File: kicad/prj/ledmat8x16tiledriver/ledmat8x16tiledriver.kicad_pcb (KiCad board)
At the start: 4 copper layers, 31.9 x 31.9 mm, 15 parts, among them J3 Conn_02x08_Odd_Even, J4 Conn_02x08_Odd_Even, U2 DMP31D7LDW, U3 DMP31D7LDW, U4 DMP31D7LDW, U5 DMP31D7LDW

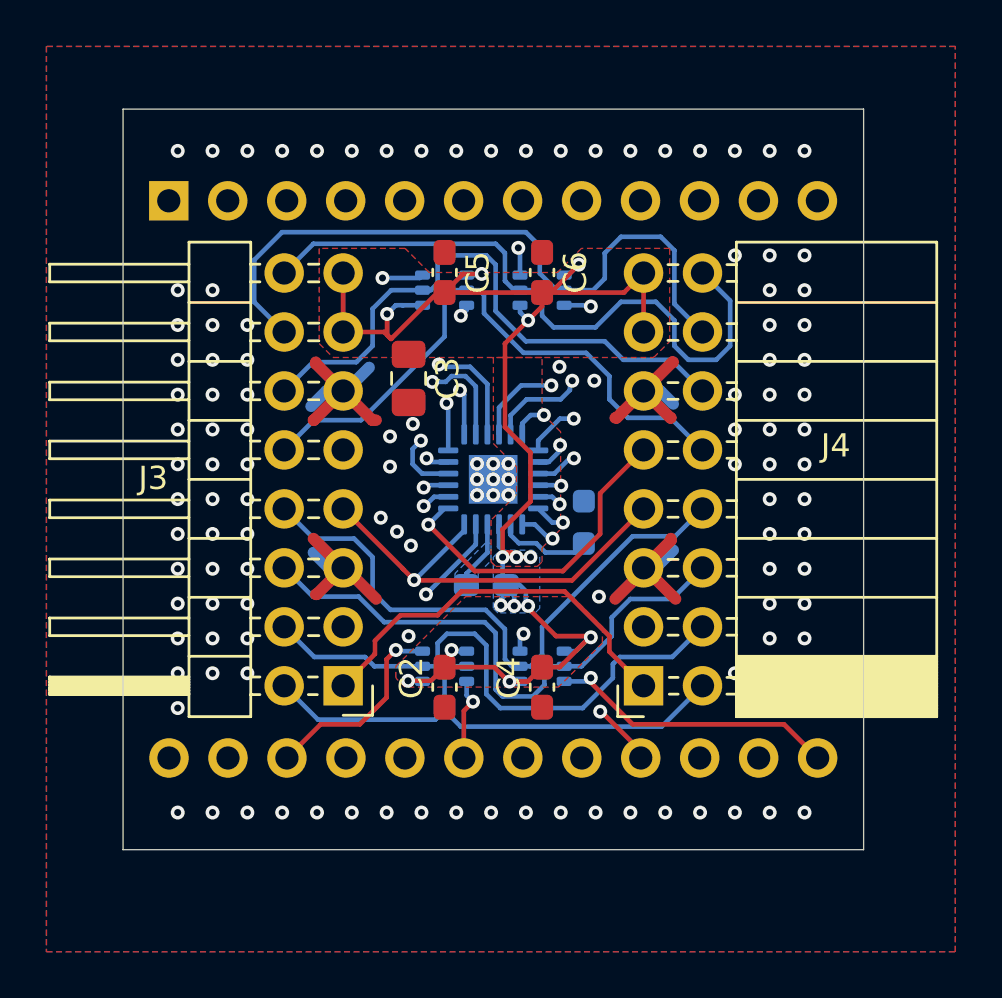
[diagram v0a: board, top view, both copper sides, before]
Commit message: re-route traces close to clock trace
Clock appeared to couple into the closeby traces
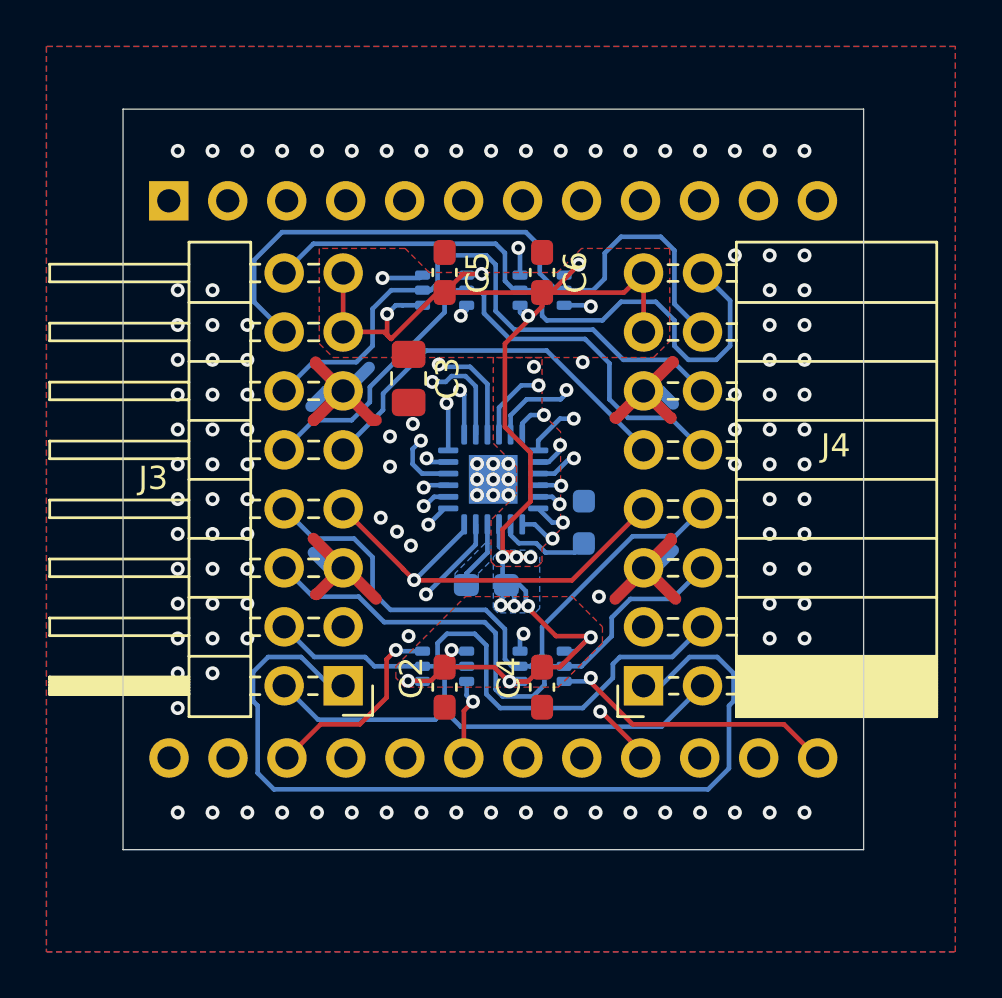
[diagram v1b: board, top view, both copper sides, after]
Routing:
- net /BLANK: track 41.3 -> 63.1 mm
- net /LAT: track 19.4 -> 23.1 mm
- net GND: vias 126 -> 124

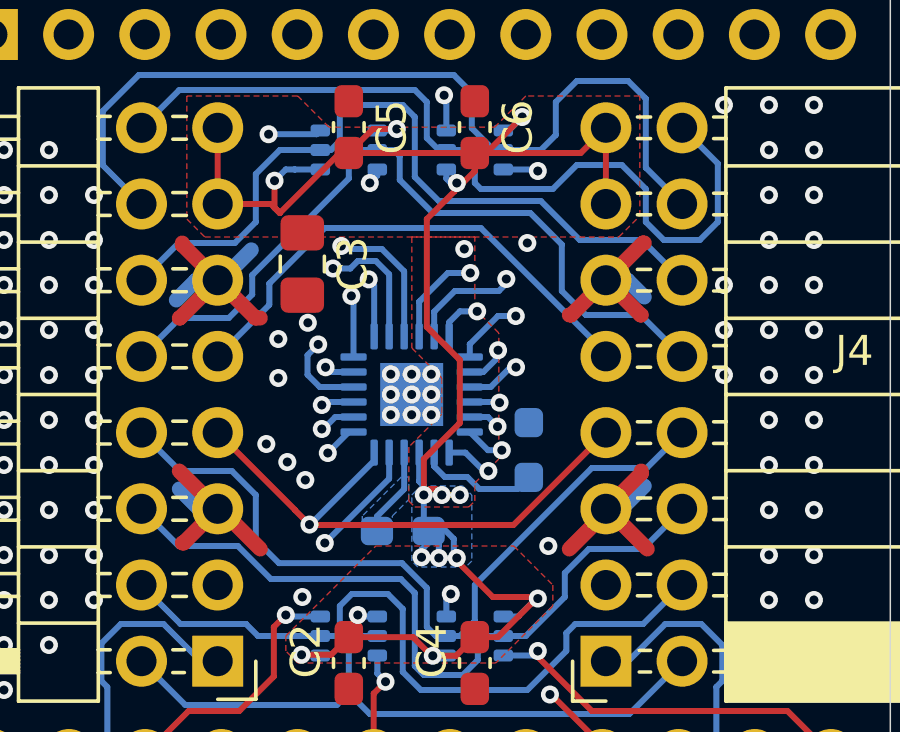
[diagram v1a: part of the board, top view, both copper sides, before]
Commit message: attempt to increase space between data and blank traces
also observed coupling of data into the blank line.
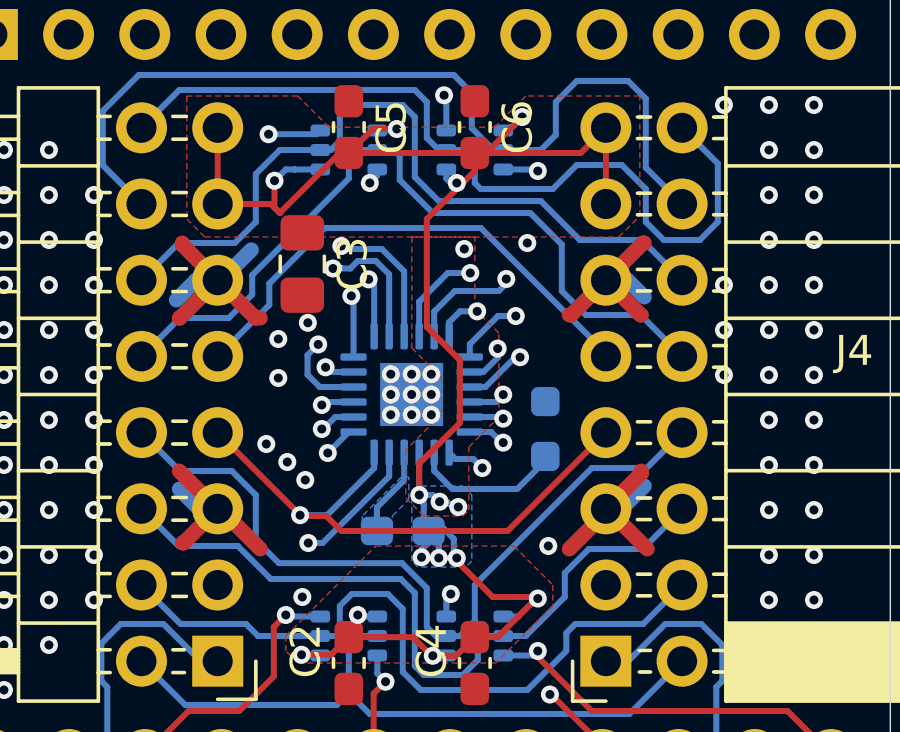
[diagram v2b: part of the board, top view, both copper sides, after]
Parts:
- moved R9 0.89 mm to (149.6, 76.3)
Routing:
- net Net-(U1-IREF): track 4.09 -> 5.10 mm
- net Net-(U1-OUT13): track 20.2 -> 21.0 mm
- net Net-(U1-OUT14): track 26.2 -> 26.7 mm
